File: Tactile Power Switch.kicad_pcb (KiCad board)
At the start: 2 copper layers, 11 parts, among them J1 OSTTC020162, J2 OSTTC020162, Q1 BC847B_215, Q2 BC847B_215, Q3 DMG2305UX-13

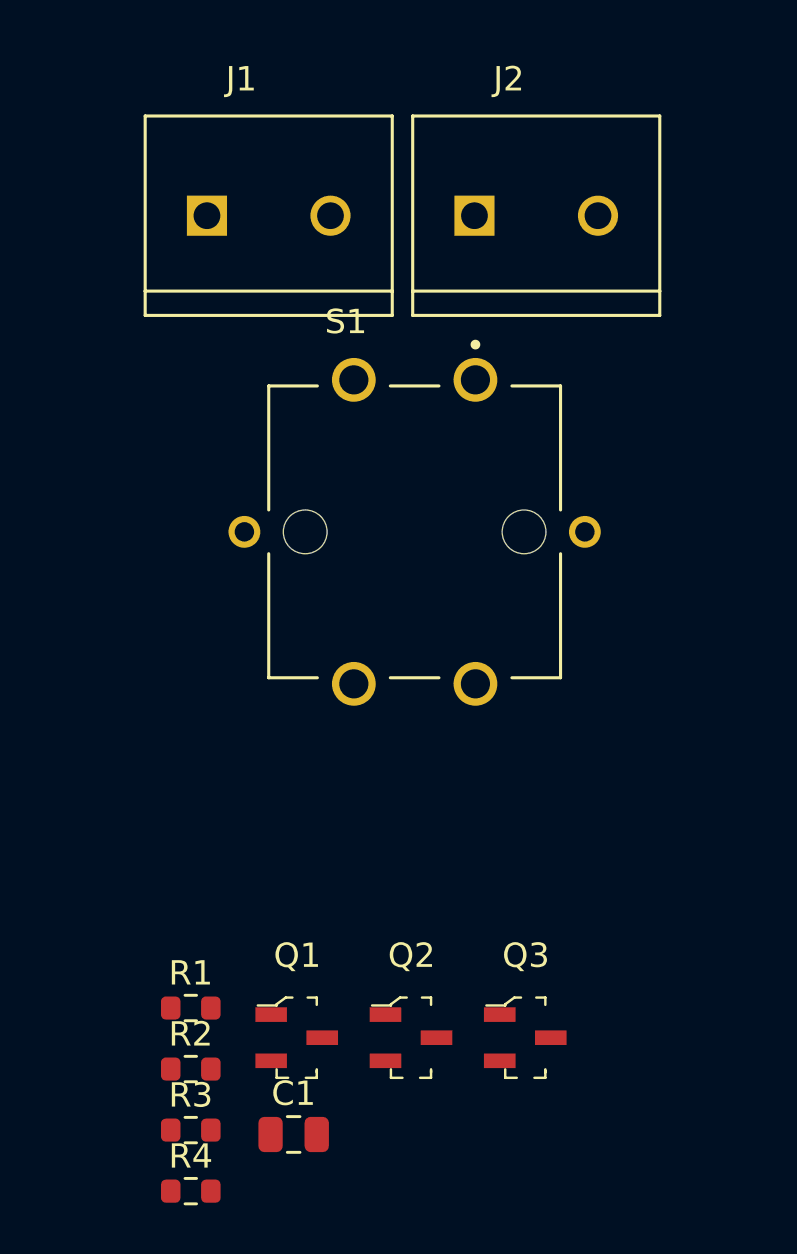
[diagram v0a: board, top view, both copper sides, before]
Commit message: Initial component placement
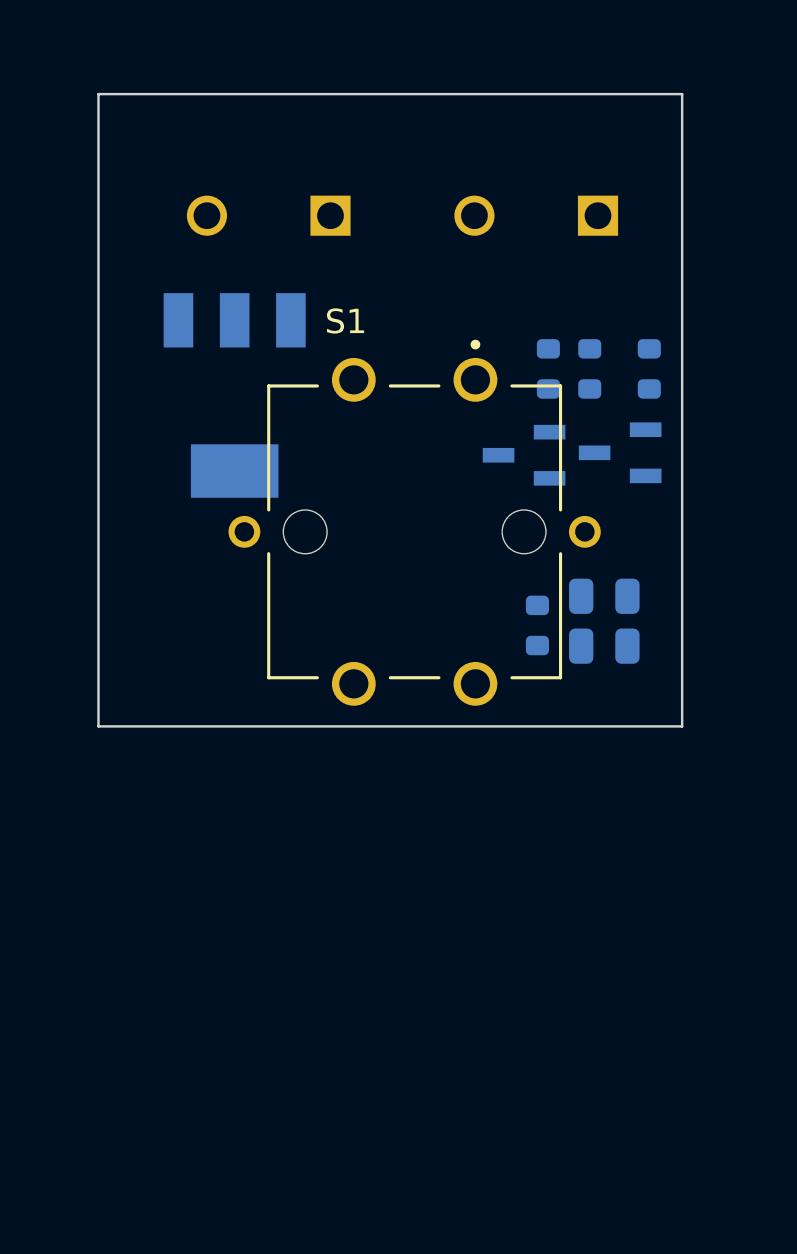
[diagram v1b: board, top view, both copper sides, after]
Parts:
- removed Q3: DMG2305UX-13, digikey-footprints:SOT-23-3
- added C2: 22uF, Capacitor_SMD:C_0805_2012Metric, B.Cu at (130.8, 67.7)
- added Q4: NDT2955, MOSFET:SOT223, B.Cu at (115.6, 57.4)
- C1, J1, J2, Q1, Q2, R1, R2, R3, R4: moved to B.Cu
- moved R3 34.6 mm to (128.5, 56.3), turned to -90 degrees
- moved R2 34.4 mm to (132.7, 56.3), turned to -90 degrees
- moved R1 31.0 mm to (130.2, 56.3), turned to 90 degrees
- moved Q1 27.5 mm to (131.4, 59.7), turned to 180 degrees
- moved R4 27.3 mm to (128.1, 66.8), turned to -90 degrees
- moved C1 25.6 mm to (130.8, 65.7)
- moved Q2 24.4 mm to (127.5, 59.8), turned to 180 degrees
- turned J1 to 180 degrees
- turned J2 to 180 degrees
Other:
- board outline added: 24 x 26 mm

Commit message: Placement Finished
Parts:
- added H1: MountingHole, MountingHole:MountingHole_2.7mm_M2.5_ISO7380, F.Cu at (134.0, 62.0)
- added H2: MountingHole, MountingHole:MountingHole_2.7mm_M2.5_ISO7380, F.Cu at (112.0, 62.0)
- moved Q4 14.6 mm to (116.8, 72.0), turned to 90 degrees
- moved Q1 11.5 mm to (132.0, 71.2)
- moved Q2 11.4 mm to (128.0, 71.2)
- moved R1 11.3 mm to (131.3, 67.5)
- moved R3 11.3 mm to (129.6, 67.5)
- moved R2 11.2 mm to (133.0, 67.5)
- moved C1 9.28 mm to (128.0, 74.5)
- moved C2 9.23 mm to (128.0, 76.5)
- moved J2 1.12 mm to (129.0, 50.5), turned to 0 degrees
- moved S1 1.00 mm to (123.0, 62.0)
- moved R4 0.65 mm to (128.0, 67.5)
- moved J1 0.50 mm to (117.0, 50.5), turned to 0 degrees
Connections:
- net +5V renamed +12V
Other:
- board size 24 x 26 mm -> 27.4 x 32 mm

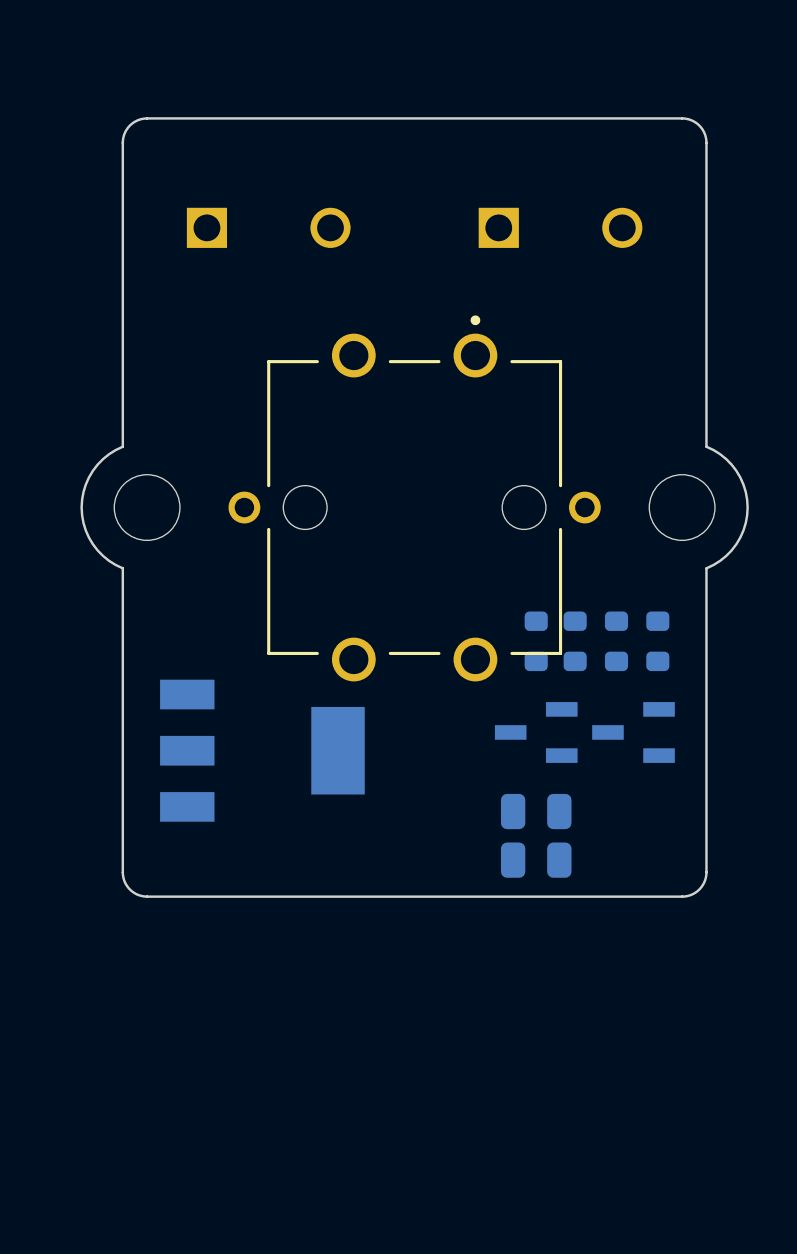
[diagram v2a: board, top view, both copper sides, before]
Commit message: Palcement Change, Screw Terminal footfrint change to 2.54 inch and overall pcb outline optimization
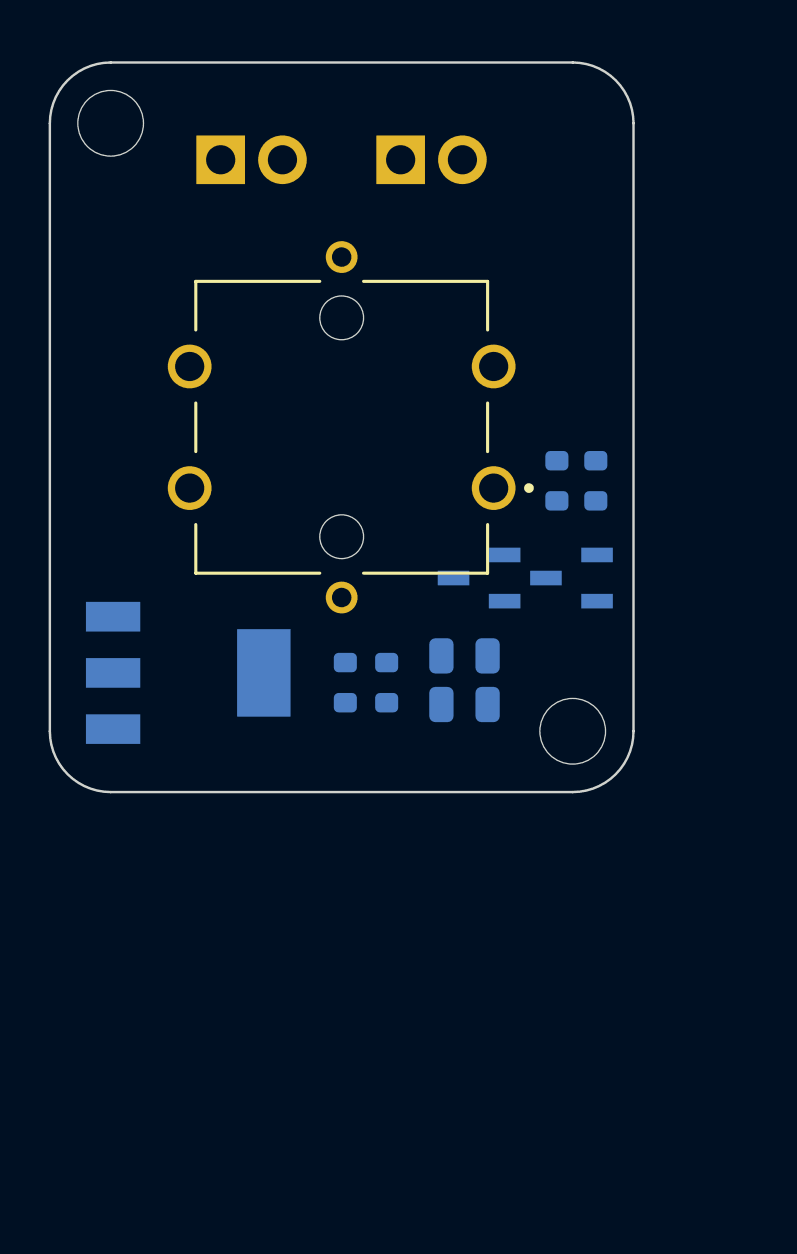
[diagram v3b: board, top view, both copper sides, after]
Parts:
- J1, J2: footprint Screw_Terminal:Screw_Terminal-2_pins -> TerminalBlock:TerminalBlock_Xinya_XY308-2.54-2P_1x02_P2.54mm_Horizontal
- moved H2 15.9 mm to (110.5, 46.2)
- moved R2 11.3 mm to (121.8, 69.2), turned to 90 degrees
- moved H1 10.2 mm to (129.5, 71.2)
- moved R4 8.03 mm to (120.2, 69.2)
- moved J2 7.15 mm to (122.4, 47.7)
- moved C1 7.05 mm to (125.0, 68.1)
- moved C2 7.05 mm to (125.0, 70.1)
- moved Q1 6.84 mm to (129.4, 64.9)
- moved Q2 6.77 mm to (125.7, 64.9)
- moved R1 6.65 mm to (130.4, 60.9)
- moved R3 6.64 mm to (128.8, 60.9)
- moved S1 4.46 mm to (120.0, 58.7), turned to -90 degrees
- moved Q4 4.42 mm to (113.7, 68.8)
- moved J1 3.43 mm to (115.0, 47.7)
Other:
- board size 27.4 x 32 mm -> 24 x 30 mm

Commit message: Initial Layout Finished - Next step to add silkscreen and final check
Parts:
- moved C1 0.30 mm to (125.0, 68.4)
- moved C2 0.30 mm to (125.0, 70.4)
- moved R1 0.30 mm to (130.4, 61.2)
- moved R3 0.30 mm to (128.8, 61.2)
- moved H1 0.30 mm to (129.5, 71.5)
- moved H2 0.30 mm to (110.5, 46.5)
- moved J1 0.30 mm to (115.0, 48.0)
- moved J2 0.30 mm to (122.4, 48.0)
- moved Q1 0.30 mm to (129.4, 65.2)
- moved Q2 0.30 mm to (125.7, 65.2)
- moved Q4 0.30 mm to (113.7, 69.1)
- moved R2 0.30 mm to (121.8, 69.5)
- moved R4 0.30 mm to (120.2, 69.5)
- moved S1 0.30 mm to (120.0, 59.0)
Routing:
- net +12V: track 0.00 -> 52.2 mm
- net VDD: track 0.00 -> 40.8 mm
- net Net-(Q1-B): track 0.00 -> 36.5 mm, vias 0 -> 1
- net Net-(Q1-C): track 0.00 -> 32.5 mm
- net Net-(Q2-C): track 0.00 -> 25.8 mm, vias 0 -> 1
- net GND: track 0.00 -> 5.20 mm, vias 0 -> 4
- net Net-(R4-Pad1): track 0.00 -> 2.74 mm
- added copper zone on B.Cu, net GND
- added copper zone on F.Cu, net GND

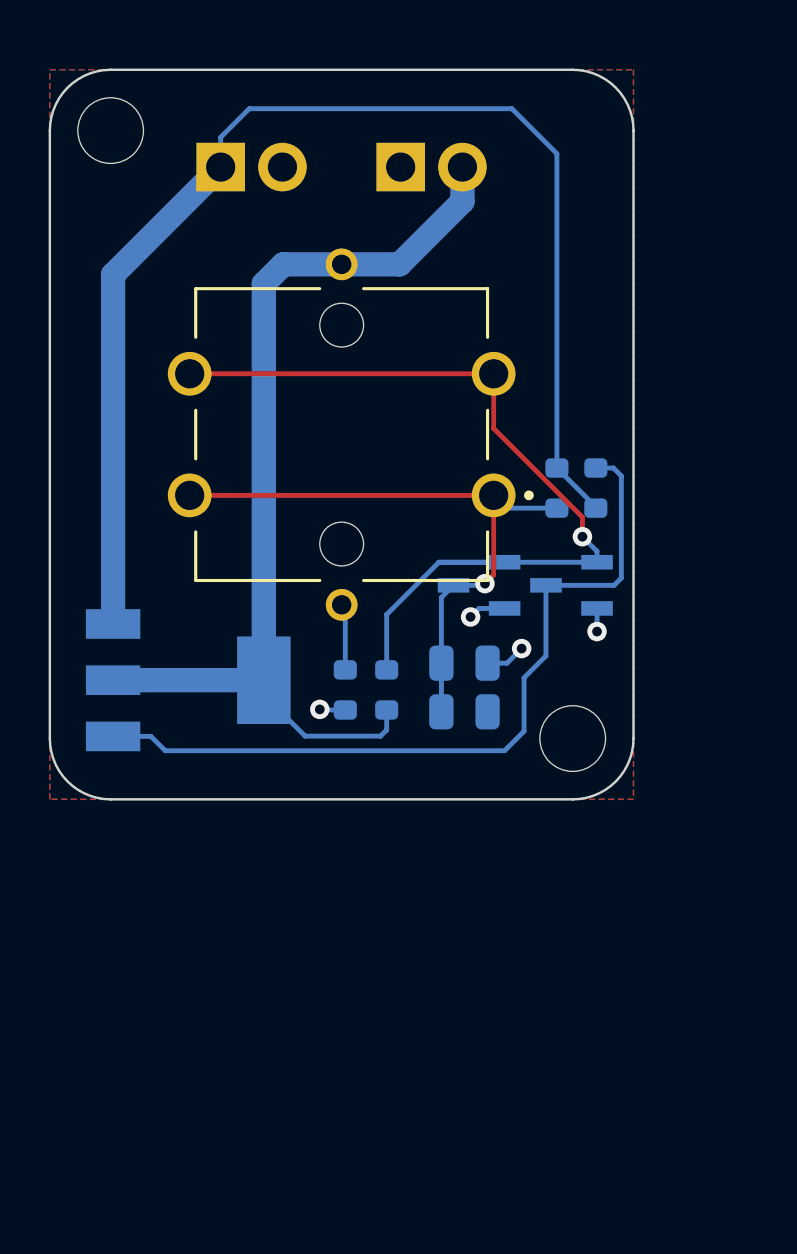
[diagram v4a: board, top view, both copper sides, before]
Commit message: Silkscreen logos and description added
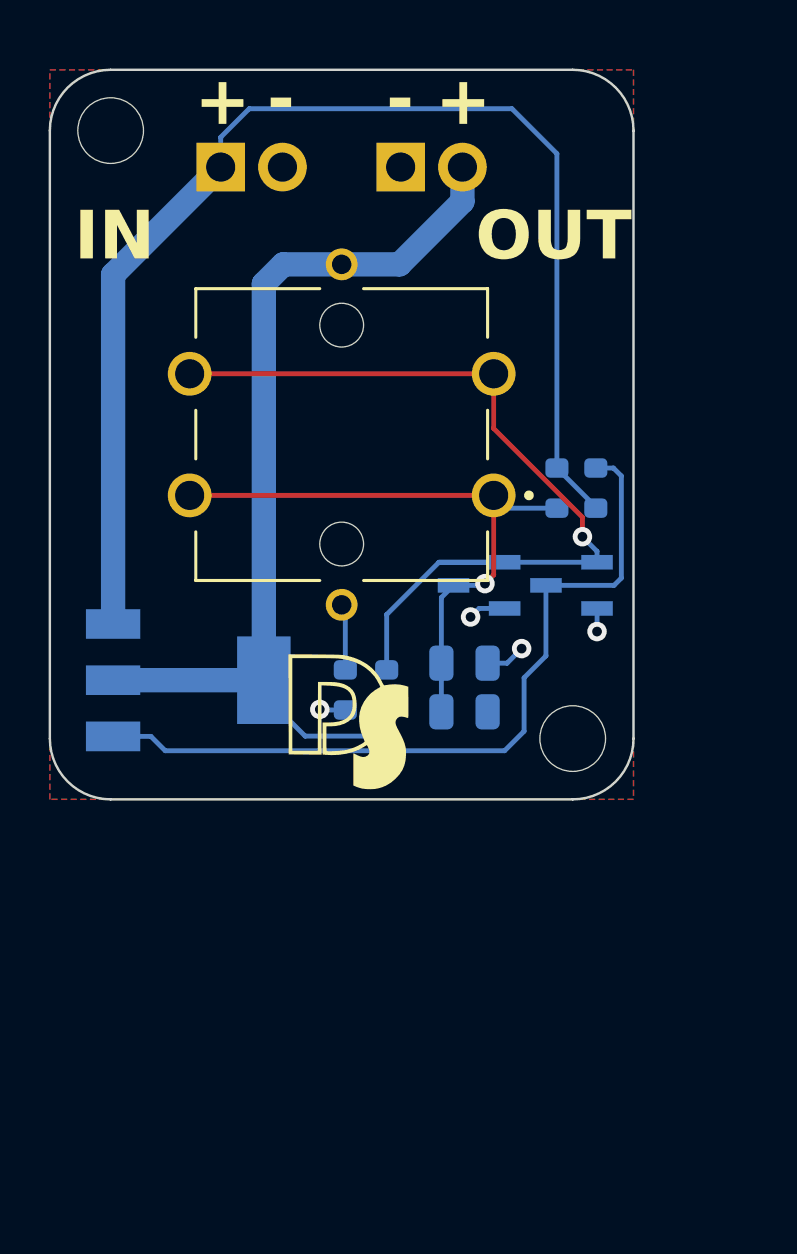
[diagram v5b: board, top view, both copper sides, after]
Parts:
- added G***: LOGO, logos:DS_logo_6x6mm, F.Cu at (120.3, 70.8)
- added G***: LOGO, logos:one_suns_4x4mm, B.Cu at (120.0, 59.0)
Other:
- board text added: "+"
- board text added: "-"
- board text added: "IN"
- board text added: "OUT"

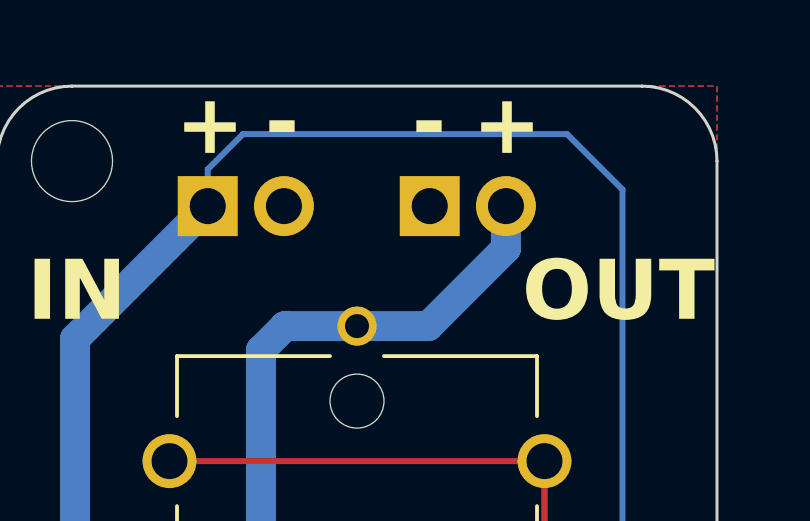
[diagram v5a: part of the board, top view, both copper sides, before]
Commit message: Terminal output connector configureation change
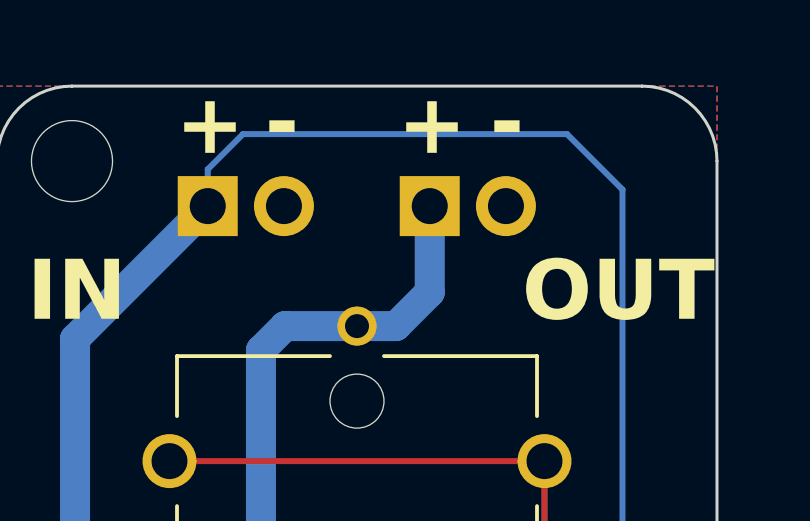
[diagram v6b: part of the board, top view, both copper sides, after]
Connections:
- J2 pad 1: GND -> VDD
- J2 pad 2: VDD -> GND
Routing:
- net VDD: track 40.8 -> 39.1 mm
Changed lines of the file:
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@@
 			(layers "*.Cu" "*.Mask")
 			(remove_unused_layers no)
-			(net 2 "GND")
+			(net 4 "VDD")
 			(pintype "passive")
 		)
@@
 			(layers "*.Cu" "*.Mask")
 			(remove_unused_layers no)
-			(net 4 "VDD")
+			(net 2 "GND")
 			(pintype "passive")
 		)
@@
 		)
 	)
-	(gr_text "+"
-		(at 127.7 45 180)
-		(layer "B.SilkS")
-		(effects
-			(font
-				(face "Segoe UI Black")
-				(size 2 2)
-				(thickness 0.2)
-				(bold yes)
-			)
-			(justify mirror)
-		)
-		(render_cache "+" 180
-			(polygon
-				(pts
-					(xy 127.875855 44.800146) (xy 127.875855 44.295052) (xy 127.534892 44.295052) (xy 127.534892 44.800146)
-					(xy 127.026378 44.800146) (xy 127.026378 45.139155) (xy 127.534892 45.139155) (xy 127.534892 45.639364)
-					(xy 127.875855 45.639364) (xy 127.875855 45.139155) (xy 128.388277 45.139155) (xy 128.388277 44.800146)
-				)
-			)
-		)
-	)
 	(gr_text "IN"
 		(at 110.7 48.9 90)
@@
 	)
 	(gr_text "-"
-		(at 119.8 45 180)
+		(at 127.6 45 180)
 		(layer "B.SilkS")
 		(effects
@@
 			(polygon
 				(pts
-					(xy 119.426797 44.701472) (xy 119.426797 45.107892) (xy 120.178576 45.107892) (xy 120.178576 44.701472)
+					(xy 127.226797 44.701472) (xy 127.226797 45.107892) (xy 127.978576 45.107892) (xy 127.978576 44.701472)
 				)
 			)
@@
 	)
 	(gr_text "+"
-		(at 125 45.3 0)
+		(at 122.5 45.3 0)
 		(layer "F.SilkS")
 		(effects
@@
 			(polygon
 				(pts
-					(xy 125.175855 45.499853) (xy 125.175855 46.004947) (xy 124.834892 46.004947) (xy 124.834892 45.499853)
-					(xy 124.326378 45.499853) (xy 124.326378 45.160844) (xy 124.834892 45.160844) (xy 124.834892 44.660635)
-					(xy 125.175855 44.660635) (xy 125.175855 45.160844) (xy 125.688277 45.160844) (xy 125.688277 45.499853)
+					(xy 122.675855 45.499853) (xy 122.675855 46.004947) (xy 122.334892 46.004947) (xy 122.334892 45.499853)
+					(xy 121.826378 45.499853) (xy 121.826378 45.160844) (xy 122.334892 45.160844) (xy 122.334892 44.660635)
+					(xy 122.675855 44.660635) (xy 122.675855 45.160844) (xy 123.188277 45.160844) (xy 123.188277 45.499853)
 				)
 			)
@@
 	)
 	(gr_text "-"
-		(at 122.4 45.2 0)
+		(at 125 45.2 0)
 		(layer "F.SilkS")
 		(effects
@@
 			(polygon
 				(pts
-					(xy 122.026797 45.498527) (xy 122.026797 45.092107) (xy 122.778576 45.092107) (xy 122.778576 45.498527)
+					(xy 124.626797 45.498527) (xy 124.626797 45.092107) (xy 125.378576 45.092107) (xy 125.378576 45.498527)
 				)
 			)
@@
 	)
 	(segment
+		(start 122.425 50.875)
+		(end 122.425 48)
+		(width 1)
+		(layer "B.Cu")
+		(net 4)
+	)
+	(segment
 		(start 120 52.000001)
-		(end 122.379212 52.000001)
+		(end 121.299999 52.000001)
 		(width 1)
 		(layer "B.Cu")
@@
 	)
 	(segment
-		(start 122.379212 52.000001)
-		(end 124.965 49.414213)
+		(start 121.299999 52.000001)
+		(end 122.425 50.875)
 		(width 1)
 		(layer "B.Cu")
@@
 		(width 1)
 		(layer "B.Cu")
-		(net 4)
-	)
-	(segment
-		(start 124.965 49.414213)
-		(end 124.965 48)
-		(width 1)
-		(layer "B.Cu")

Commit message: SMD version: Placement is done
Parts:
- removed S1: TSD1265, SW_TSD1265:SW_TSD1265
- added D1: GREEN, LED_SMD:LED_0603_1608Metric, F.Cu at (128.0, 59.0)
- added SW1: SW_SPST, Button_Switch_SMD:SW_SPST_TL3342, F.Cu at (120.0, 59.0)
- C1, C2, Q1, Q2, R1, R2, R3, R4: moved to F.Cu
- Q4: footprint MOSFET:SOT223 -> Package_TO_SOT_SMD:SOT-223; moved to F.Cu
- moved R4 16.3 mm to (127.2, 54.8), turned to 180 degrees
- moved R2 14.1 mm to (127.2, 56.5), turned to 180 degrees
- moved R1 10.8 mm to (121.7, 67.5)
- moved R3 9.05 mm to (124.1, 68.9), turned to 0 degrees
- moved Q1 6.07 mm to (123.5, 64.0), turned to -90 degrees
- moved C1 3.65 mm to (127.8, 66.0)
- moved C2 3.48 mm to (124.3, 67.0), turned to 180 degrees
- moved Q4 3.36 mm to (115.0, 66.0), turned to 0 degrees
- moved J1 3.13 mm to (117.3, 50.1)
- moved Q2 3.08 mm to (127.8, 63.0), turned to 0 degrees
- moved J2 2.67 mm to (124.0, 50.1)
- moved H1 2.24 mm to (128.5, 69.5)
- moved H2 2.24 mm to (111.5, 48.5)
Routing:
- net +12V: track 52.2 -> 0.00 mm
- net VDD: track 39.1 -> 0.00 mm
- net Net-(Q1-B): track 36.5 -> 0.00 mm, vias 1 -> 0
- net Net-(Q1-C): track 32.5 -> 0.00 mm
- net Net-(Q2-C): track 25.8 -> 0.00 mm, vias 1 -> 0
- net GND: track 5.20 -> 0.00 mm, vias 4 -> 0
- net Net-(D1-K): track 2.74 -> 0.00 mm
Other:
- board size 24 x 30 mm -> 22 x 26 mm
